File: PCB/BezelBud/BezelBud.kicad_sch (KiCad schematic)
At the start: 40 parts, among them J1 USB_C_Receptacle_USB2.0_16P, J2 Conn_01x05_Pin, SW1 SW_SPDT, SW2 SW_SPDT, U1 USBLC6-2SC6, U2 STM32G431CBT6, U3 LP5907MFX-3.3, U4 GSA4030H10-B26-5P, Y1 Crystal_GND24

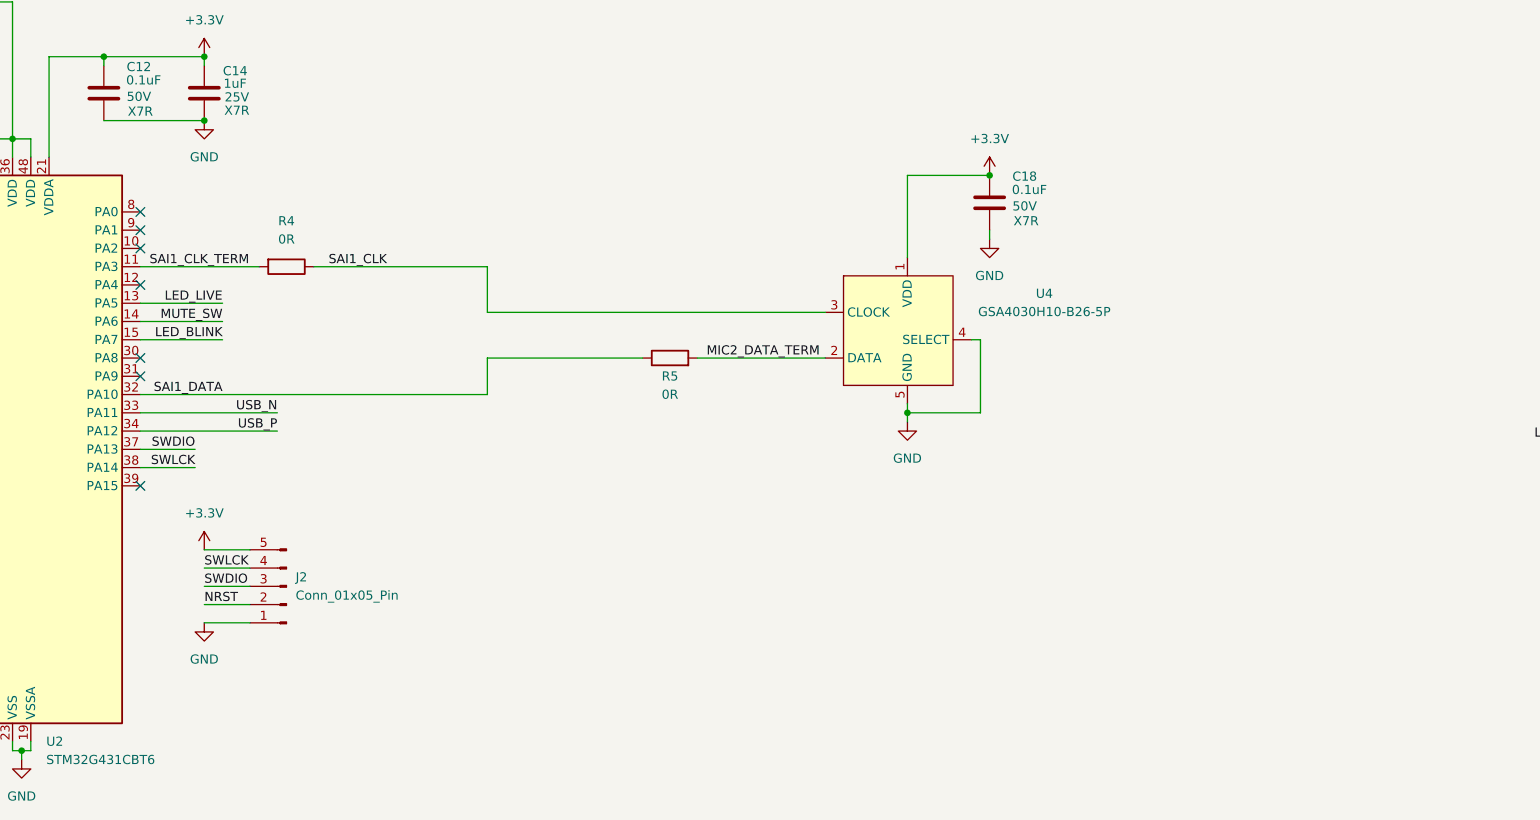
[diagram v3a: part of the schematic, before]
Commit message: updated footprints for mic and debug
started pcb layout
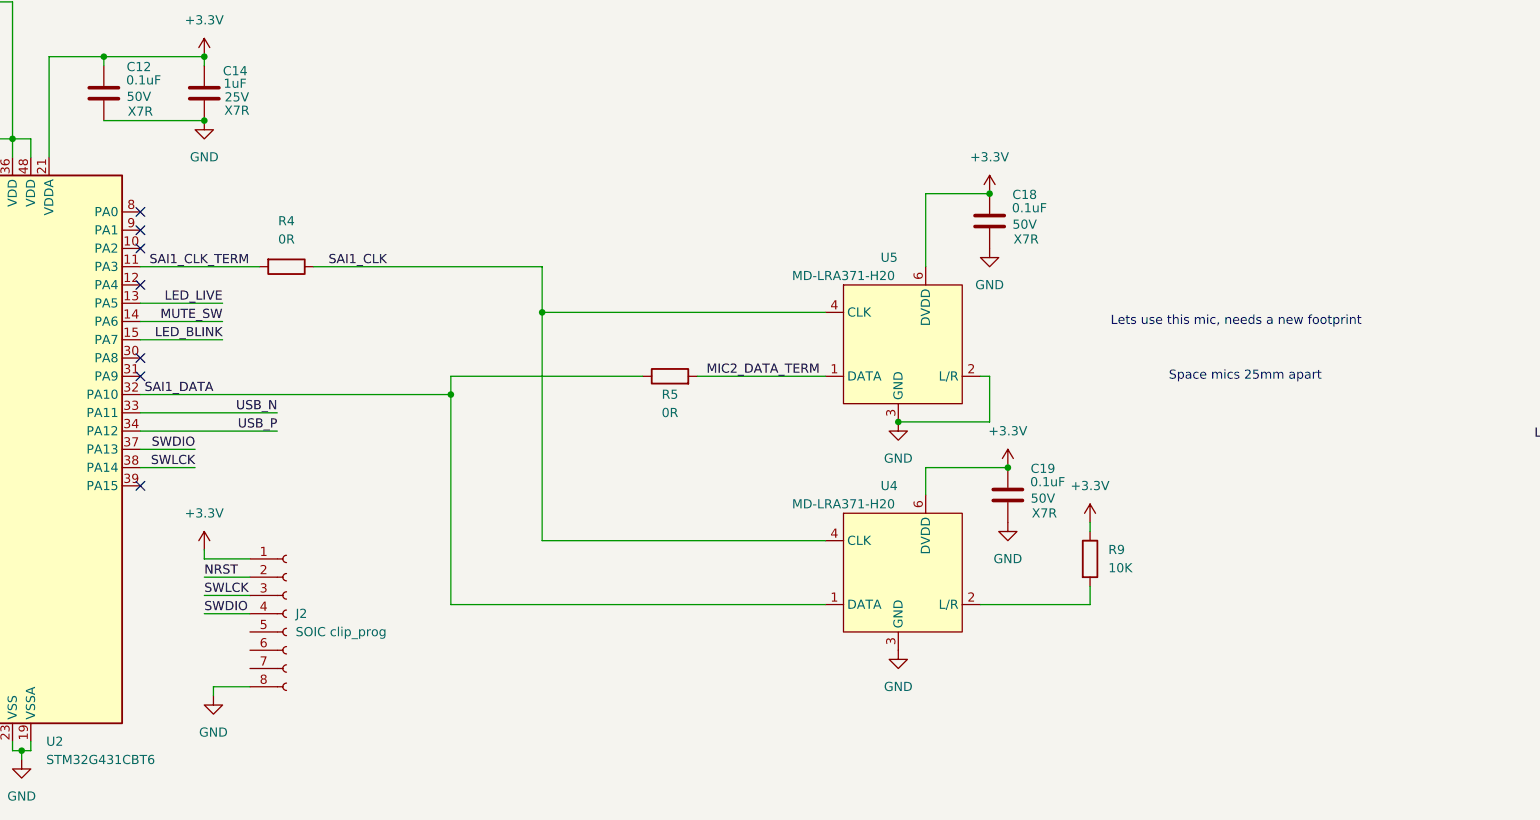
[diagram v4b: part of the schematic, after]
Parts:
- removed J2: Conn_01x05_Pin, Connector_PinHeader_2.54mm:PinHeader_1x05_P2.54mm_Vertical, symbol Connector:Conn_01x05_Pin
- removed U4: GSA4030H10-B26-5P, BevelBud:GSA4030H10-B26-5P, symbol BevelBud:GSA4030H10-B26-5P
- added C19: 0.1uF, Capacitor_SMD:C_0603_1608Metric, symbol Device:C
- added J2: SOIC clip_prog, BevelBud:SOIC_clipProgSmall, symbol Connector:Conn_01x08_Socket
- added R9: 10K, Resistor_SMD:R_0603_1608Metric, symbol Device:R
- added U4, U5: MD-LRA371-H20, BevelBud:MD-LRA371-H20, symbol BevelBud:Gettop_MD-LRA371-H20
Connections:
- net +3.3V: now also C19.1, J2.1 (Pin_1), R9.1, U4.5 (AVDD), U4.6 (DVDD), U5.5 (AVDD), U5.6 (DVDD)
- net GND: now also C19.2, J2.8 (Pin_8), U4.3 (GND), U5.2 (L/R), U5.3 (GND)
- net MIC2_DATA_TERM: now also U5.1 (DATA)
- net NRST: now also J2.2 (Pin_2)
- net SAI1_CLK: now also U4.4 (CLK), U5.4 (CLK)
- net SAI1_DATA: now also U4.1 (DATA)
- net SWDIO: now also J2.4 (Pin_4)
- net SWLCK: now also J2.3 (Pin_3)
- new net: R9.2, U4.2 (L/R)
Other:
- note added: "Lets use this mic, needs a new footprint"
- note added: "Space mics 25mm apart"
- moved on the sheet: C18, R5

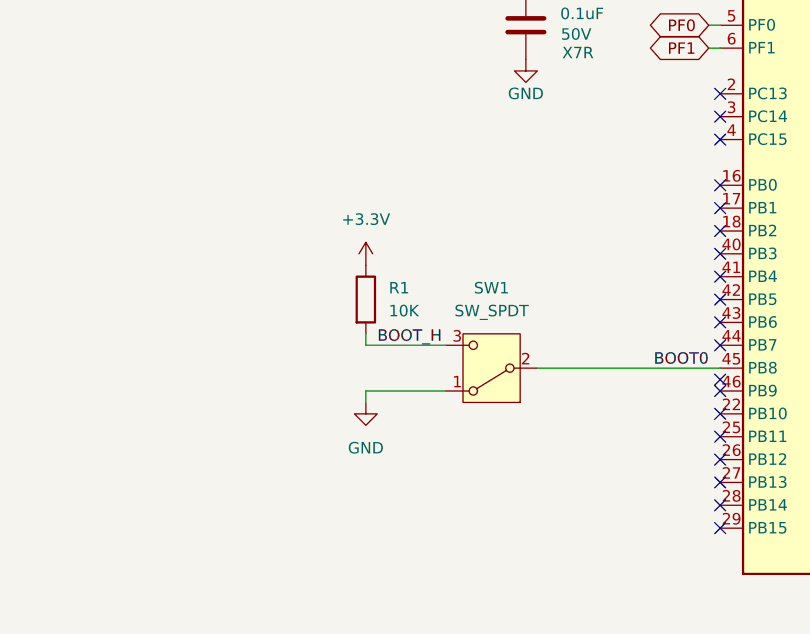
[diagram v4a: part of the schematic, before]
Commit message: Starting layout for scored and mouse bite PCB
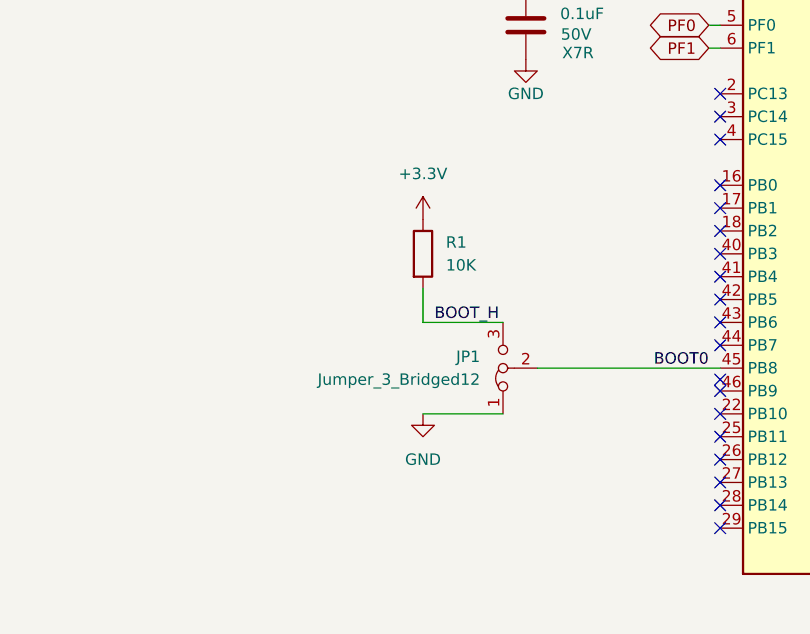
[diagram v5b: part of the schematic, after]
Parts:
- removed SW1: SW_SPDT, Connector_PinHeader_2.54mm:PinHeader_1x03_P2.54mm_Vertical, symbol Switch:SW_SPDT
- added JP1: Jumper_3_Bridged12, symbol Jumper:Jumper_3_Bridged12
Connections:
- net BOOT0: now also JP1.2 (C)
- net BOOT_H: now also JP1.3 (B)
- net GND: now also JP1.1 (A)
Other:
- moved on the sheet: R1
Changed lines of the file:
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@@
 	(wire
 		(pts
-			(xy 67.31 212.09) (xy 67.31 210.82)
+			(xy 73.66 205.74) (xy 73.66 209.55)
 		)
 		(stroke
@@
 	(wire
 		(pts
-			(xy 67.31 217.17) (xy 76.2 217.17)
+			(xy 73.66 219.71) (xy 82.55 219.71)
 		)
 		(stroke
@@
 	(wire
 		(pts
-			(xy 67.31 217.17) (xy 67.31 218.44)
-		)
-		(stroke
-			(width 0)
-			(type default)
-		)
-	)
-	(wire
-		(pts
 			(xy 85.09 171.45) (xy 85.09 172.72)
 		)
@@
 	(wire
 		(pts
-			(xy 67.31 212.09) (xy 76.2 212.09)
+			(xy 73.66 209.55) (xy 82.55 209.55)
 		)
 		(stroke
@@
 	)
 	(label "BOOT_H"
-		(at 68.58 212.09 0)
+		(at 74.93 209.55 0)
 		(effects
 			(font
@@
 					(reference "H2")
 					(unit 1)
+					(variant
+						(name "VCUT Board")
+						(dnp yes)
+						(on_board no)
+					)
 				)
 			)
@@
 	)
 	(symbol
+		(lib_id "Jumper:Jumper_3_Bridged12")
+		(at 82.55 214.63 90)
+		(unit 1)
+		(body_style 1)
+		(exclude_from_sim no)
+		(in_bom no)
+		(on_board yes)
+		(in_pos_files yes)
+		(dnp no)
+		(fields_autoplaced yes)
+		(property "Reference" "JP1"
+			(at 80.01 213.3599 90)
+			(show_name no)
+			(do_not_autoplace no)
+			(effects
+				(font
+					(size 1.27 1.27)
+				)
+				(justify left)
+			)
+		)
+		(property "Value" "Jumper_3_Bridged12"
+			(at 80.01 215.8999 90)
+			(show_name no)
+			(do_not_autoplace no)
+			(effects
+				(font
+					(size 1.27 1.27)
+				)
+				(justify left)
+			)
+		)
+		(property "Footprint" ""
+			(at 82.55 214.63 0)
+			(hide yes)
+			(show_name no)
+			(do_not_autoplace no)
+			(effects
+				(font
+					(size 1.27 1.27)
+				)
+			)
+		)
+		(property "Datasheet" ""
+			(at 82.55 214.63 0)
+			(hide yes)
+			(show_name no)
+			(do_not_autoplace no)
+			(effects
+				(font
+					(size 1.27 1.27)
+				)
+			)
+		)
+		(property "Description" "Jumper, 3-pole, pins 1+2 closed/bridged"
+			(at 93.98 214.63 0)
+			(hide yes)
+			(show_name no)
+			(do_not_autoplace no)
+			(effects
+				(font
+					(size 1.27 1.27)
+				)
+			)
+		)
+		(pin "1"
+		)
+		(pin "2"
+		)
+		(pin "3"
+		)
+		(instances
+			(project "BezelBud"
+				(path "/ea52eff0-b87d-4555-a937-35a2be025cf5"
+					(reference "JP1")
+					(unit 1)
+					(variant
+						(name "VCUT Board")
+						(field
+							(name "Footprint")
+							(value "Jumper:SolderJumper-3_P1.3mm_Open_RoundedPad1.0x1.5mm")
+						)
+					)
+				)
+			)
+		)
+	)
+	(symbol
 		(lib_id "MCU_ST_STM32G4:STM32G431CBTx")
 		(at 124.46 199.39 0)
@@
 	(symbol
 		(lib_id "power:GND")
-		(at 67.31 218.44 0)
+		(at 73.66 219.71 0)
 		(unit 1)
 		(body_style 1)
@@
 		(fields_autoplaced yes)
 		(property "Reference" "#PWR06"
-			(at 67.31 224.79 0)
+			(at 73.66 226.06 0)
 			(hide yes)
 			(show_name no)
@@
 		)
 		(property "Value" "GND"
-			(at 67.31 223.52 0)
+			(at 73.66 224.79 0)
 			(show_name no)
 			(do_not_autoplace no)
@@
 		)
 		(property "Footprint" ""
-			(at 67.31 218.44 0)
+			(at 73.66 219.71 0)
 			(hide yes)
 			(show_name no)
@@
 		)
 		(property "Datasheet" ""
-			(at 67.31 218.44 0)
+			(at 73.66 219.71 0)
 			(hide yes)
 			(show_name no)
@@
 		)
 		(property "Description" "Power symbol creates a global label with name \"GND\" , ground"
-			(at 67.31 218.44 0)
+			(at 73.66 219.71 0)
 			(hide yes)
 			(show_name no)
@@
 	(symbol
 		(lib_id "power:+3.3V")
-		(at 67.31 203.2 0)
+		(at 73.66 198.12 0)
 		(unit 1)
 		(body_style 1)
@@
 		(fields_autoplaced yes)
 		(property "Reference" "#PWR05"
-			(at 67.31 207.01 0)
+			(at 73.66 201.93 0)
 			(hide yes)
 			(show_name no)
@@
 		)
 		(property "Value" "+3.3V"
-			(at 67.31 198.12 0)
+			(at 73.66 193.04 0)
 			(show_name no)
 			(do_not_autoplace no)
@@
 		)
 		(property "Footprint" ""
-			(at 67.31 203.2 0)
+			(at 73.66 198.12 0)
 			(hide yes)
 			(show_name no)
@@
 		)
 		(property "Datasheet" ""
-			(at 67.31 203.2 0)
+			(at 73.66 198.12 0)
 			(hide yes)
 			(show_name no)
@@
 		)
 		(property "Description" "Power symbol creates a global label with name \"+3.3V\""
-			(at 67.31 203.2 0)
+			(at 73.66 198.12 0)
 			(hide yes)
 			(show_name no)
@@
 	(symbol
 		(lib_id "Device:R")
-		(at 67.31 207.01 0)
+		(at 73.66 201.93 0)
 		(unit 1)
 		(body_style 1)
@@
 		(fields_autoplaced yes)
 		(property "Reference" "R1"
-			(at 69.85 205.7399 0)
+			(at 76.2 200.6599 0)
 			(show_name no)
 			(do_not_autoplace no)
@@
 		)
 		(property "Value" "10K"
-			(at 69.85 208.2799 0)
+			(at 76.2 203.1999 0)
 			(show_name no)
 			(do_not_autoplace no)
@@
 		)
 		(property "Footprint" "Resistor_SMD:R_0603_1608Metric"
-			(at 65.532 207.01 90)
+			(at 71.882 201.93 90)
 			(hide yes)
 			(show_name no)
@@
 		)
 		(property "Datasheet" ""
-			(at 67.31 207.01 0)
+			(at 73.66 201.93 0)
 			(hide yes)
 			(show_name no)
@@
 		)
 		(property "Description" "Resistor"
-			(at 67.31 207.01 0)
+			(at 73.66 201.93 0)
 			(hide yes)
 			(show_name no)
@@
 					(reference "H1")
 					(unit 1)
-				)
-			)
-		)
-	)
-	(symbol
-		(lib_id "Switch:SW_SPDT")
-		(at 81.28 214.63 180)
-		(unit 1)
-		(body_style 1)
-		(exclude_from_sim no)
-		(in_bom yes)
-		(on_board yes)
-		(in_pos_files yes)
-		(dnp no)
-		(fields_autoplaced yes)
-		(property "Reference" "SW1"
-			(at 81.28 205.74 0)
-			(show_name no)
-			(do_not_autoplace no)
-			(effects
-				(font
-					(size 1.27 1.27)
-				)
-			)
-		)
-		(property "Value" "SW_SPDT"
-			(at 81.28 208.28 0)
-			(show_name no)
-			(do_not_autoplace no)
-			(effects
-				(font
-					(size 1.27 1.27)
-				)
-			)
-		)
-		(property "Footprint" "Connector_PinHeader_2.54mm:PinHeader_1x03_P2.54mm_Vertical"
-			(at 81.28 214.63 0)
-			(hide yes)
-			(show_name no)
-			(do_not_autoplace no)
-			(effects
-				(font
-					(size 1.27 1.27)
-				)
-			)
-		)
-		(property "Datasheet" ""
-			(at 81.28 207.01 0)
-			(hide yes)
-			(show_name no)
-			(do_not_autoplace no)
-			(effects
-				(font
-					(size 1.27 1.27)
-				)
-			)
-		)
-		(property "Description" "Switch, single pole double throw"
-			(at 81.28 214.63 0)
-			(hide yes)
-			(show_name no)
-			(do_not_autoplace no)
-			(effects
-				(font
-					(size 1.27 1.27)
-				)
-			)
-		)
-		(pin "3"
-		)
-		(pin "2"
-		)
-		(pin "1"
-		)
-		(instances
-			(project "BezelBud"
-				(path "/ea52eff0-b87d-4555-a937-35a2be025cf5"
-					(reference "SW1")
-					(unit 1)
+					(variant
+						(name "VCUT Board")
+						(dnp yes)
+						(on_board no)
+						(in_pos_files no)
+					)
 				)
 			)
